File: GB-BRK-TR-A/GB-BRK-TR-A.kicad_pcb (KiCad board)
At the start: 2 copper layers, 24 x 35 mm, 7 parts, among them J1 Conn_01x04, J2 Conn_01x05, T1 GameBoy_Transformer_DMG

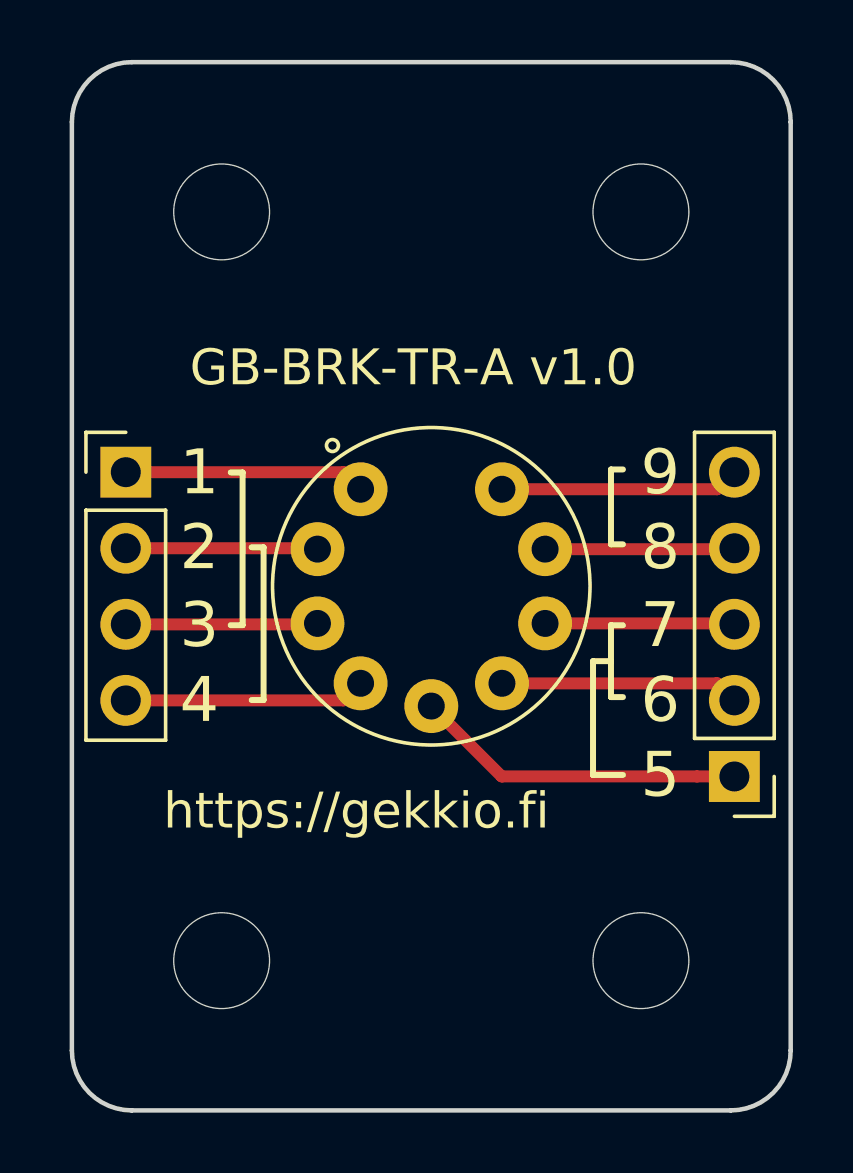
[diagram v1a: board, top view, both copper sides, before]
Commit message: Upgrade most projects to KiCad 6
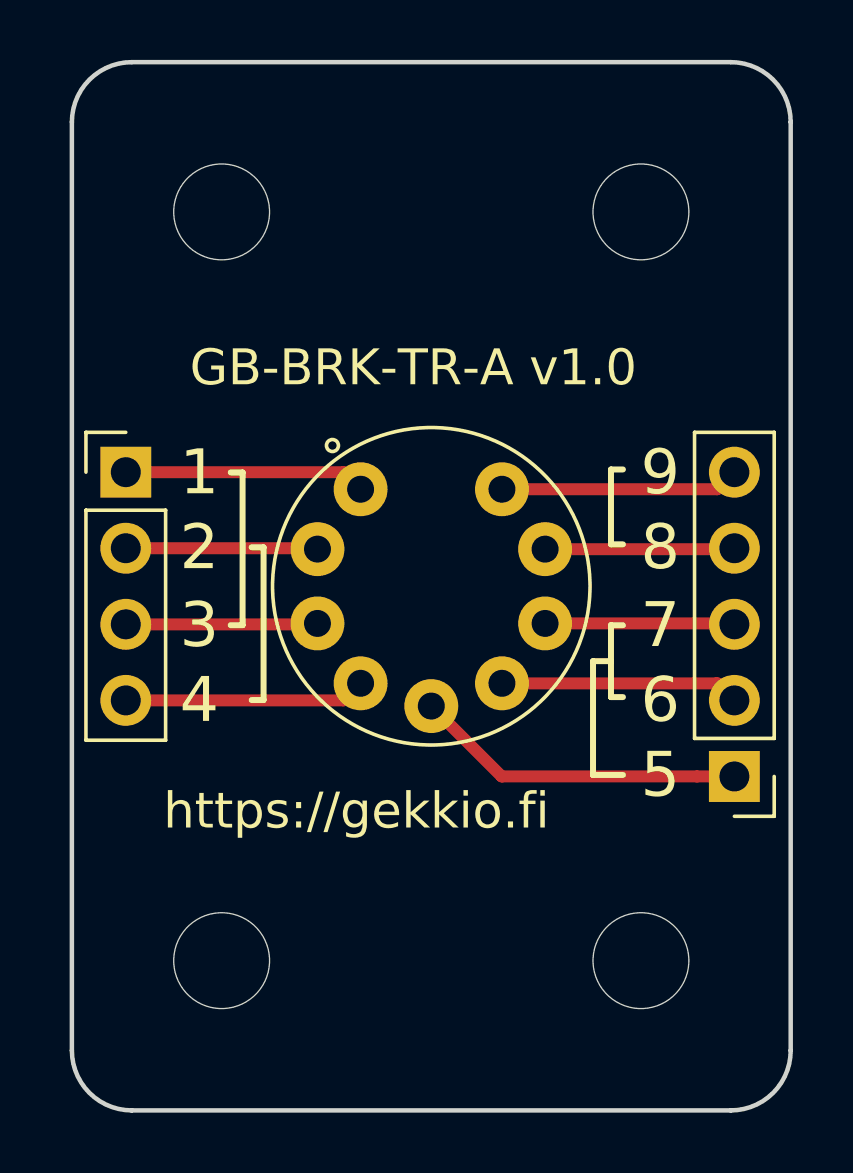
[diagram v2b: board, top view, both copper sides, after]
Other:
- net class Default removed
